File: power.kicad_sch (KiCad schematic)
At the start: 57 parts, among them Q6 2N7002K, U1 uA7805, U11 RT9080-33GJ5, U5 MIC5504, U6 DS4432U+, U6 INA219AID

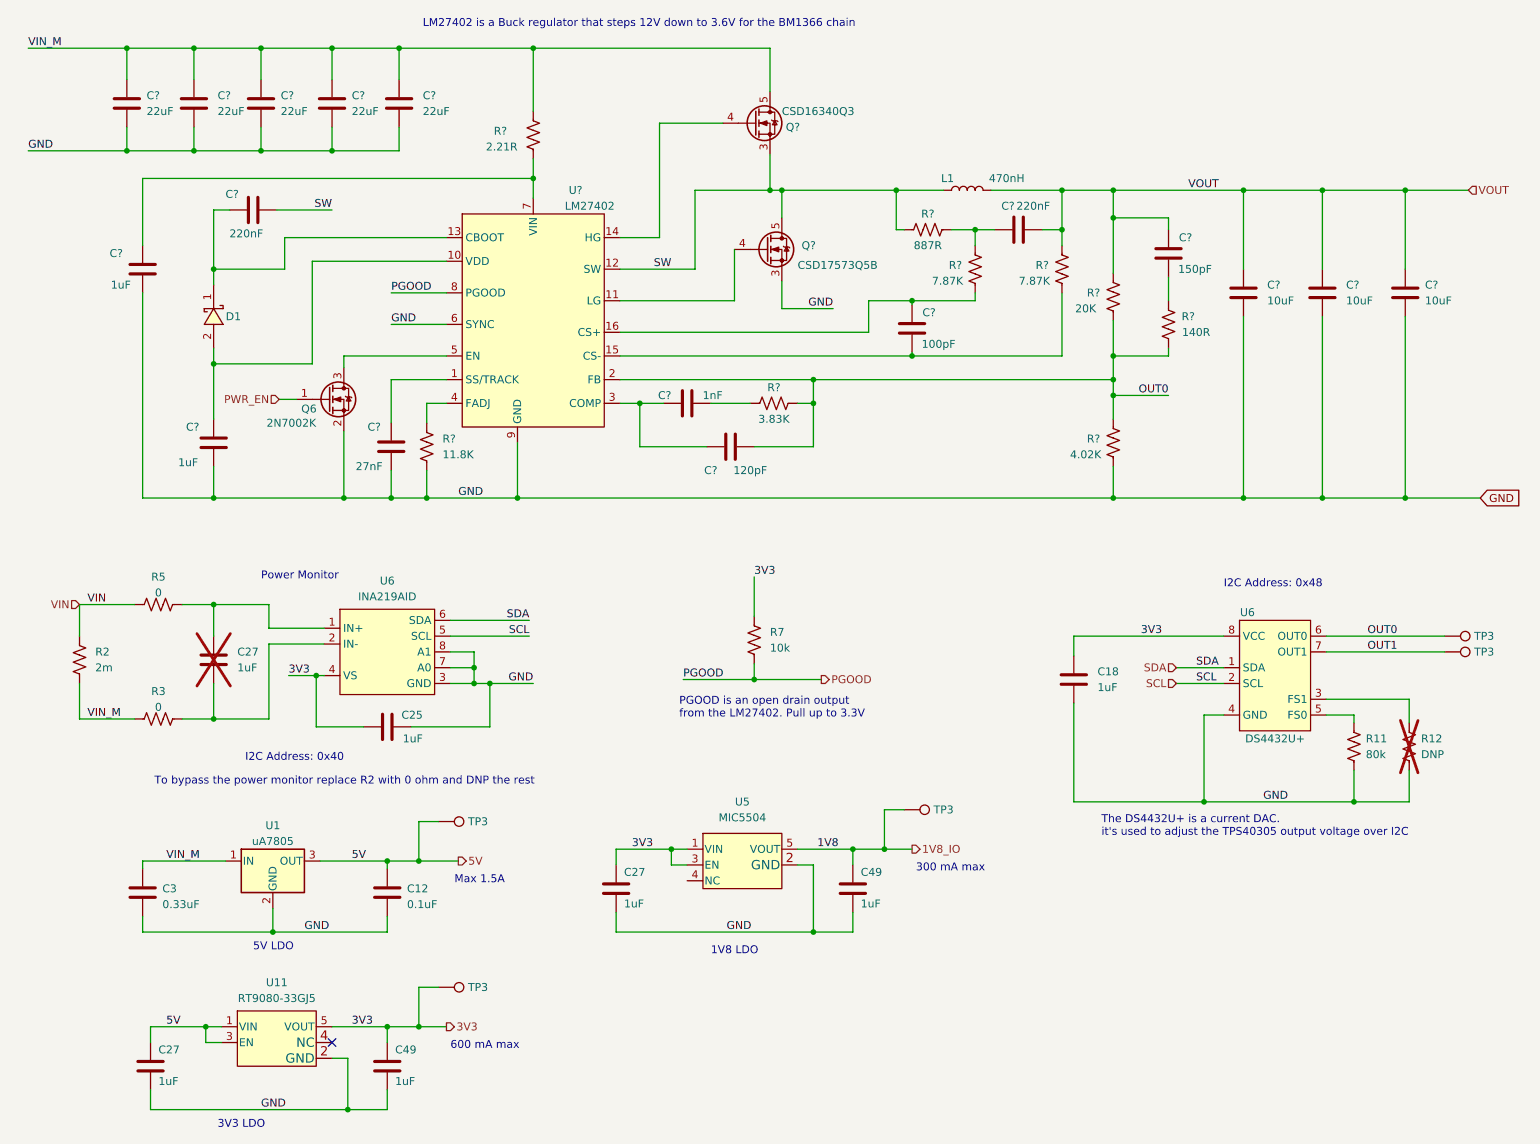
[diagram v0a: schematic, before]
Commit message: Create footprints for new MOSFETS, start on new power supply
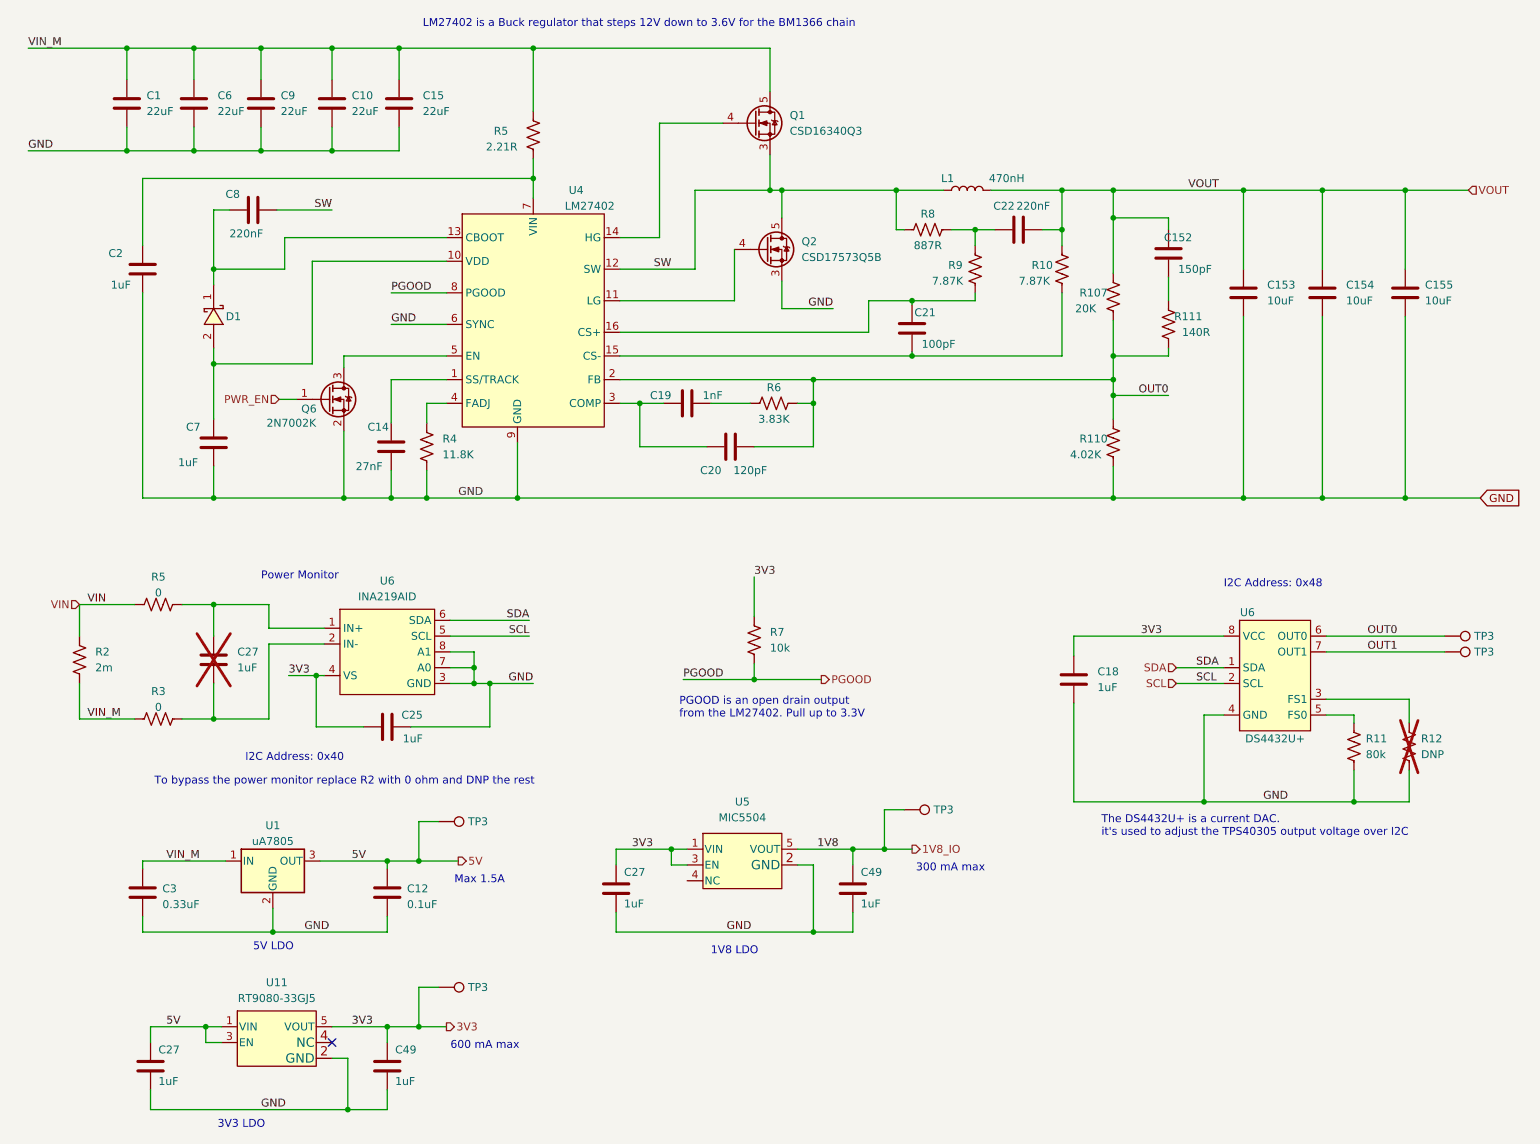
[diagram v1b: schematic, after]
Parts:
- removed Q?: CSD17573Q5B, symbol bitaxe:Q_NMOS_CSD17311Q5_1
- removed Q?: CSD16340Q3, symbol bitaxe:Q_NMOS_CSD17311Q5_1
- added Q1: CSD16340Q3, bitaxe:CSD16340Q3, symbol bitaxe:Q_NMOS_CSD16340Q3
- added Q2: CSD17573Q5B, bitaxe:CSD17573Q5B, symbol bitaxe:Q_NMOS_CSD17573Q5B
- gave numbers to parts that had none: 27
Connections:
- net GND: now also U4.17 (GND), Q2.1, Q2.2, Q2.3 (S)
- net SW: now also Q1.1, Q1.2, Q1.3 (S), Q2.5 (D)
- net VIN_M: now also Q1.5 (D)
- net at U4.11 (LG): now also Q2.4 (G)
- net at U4.14 (HG): now also Q1.4 (G)

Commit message: remove old 5V power supply, prepare footprints for new 5V buck supply, switch fans to 12V
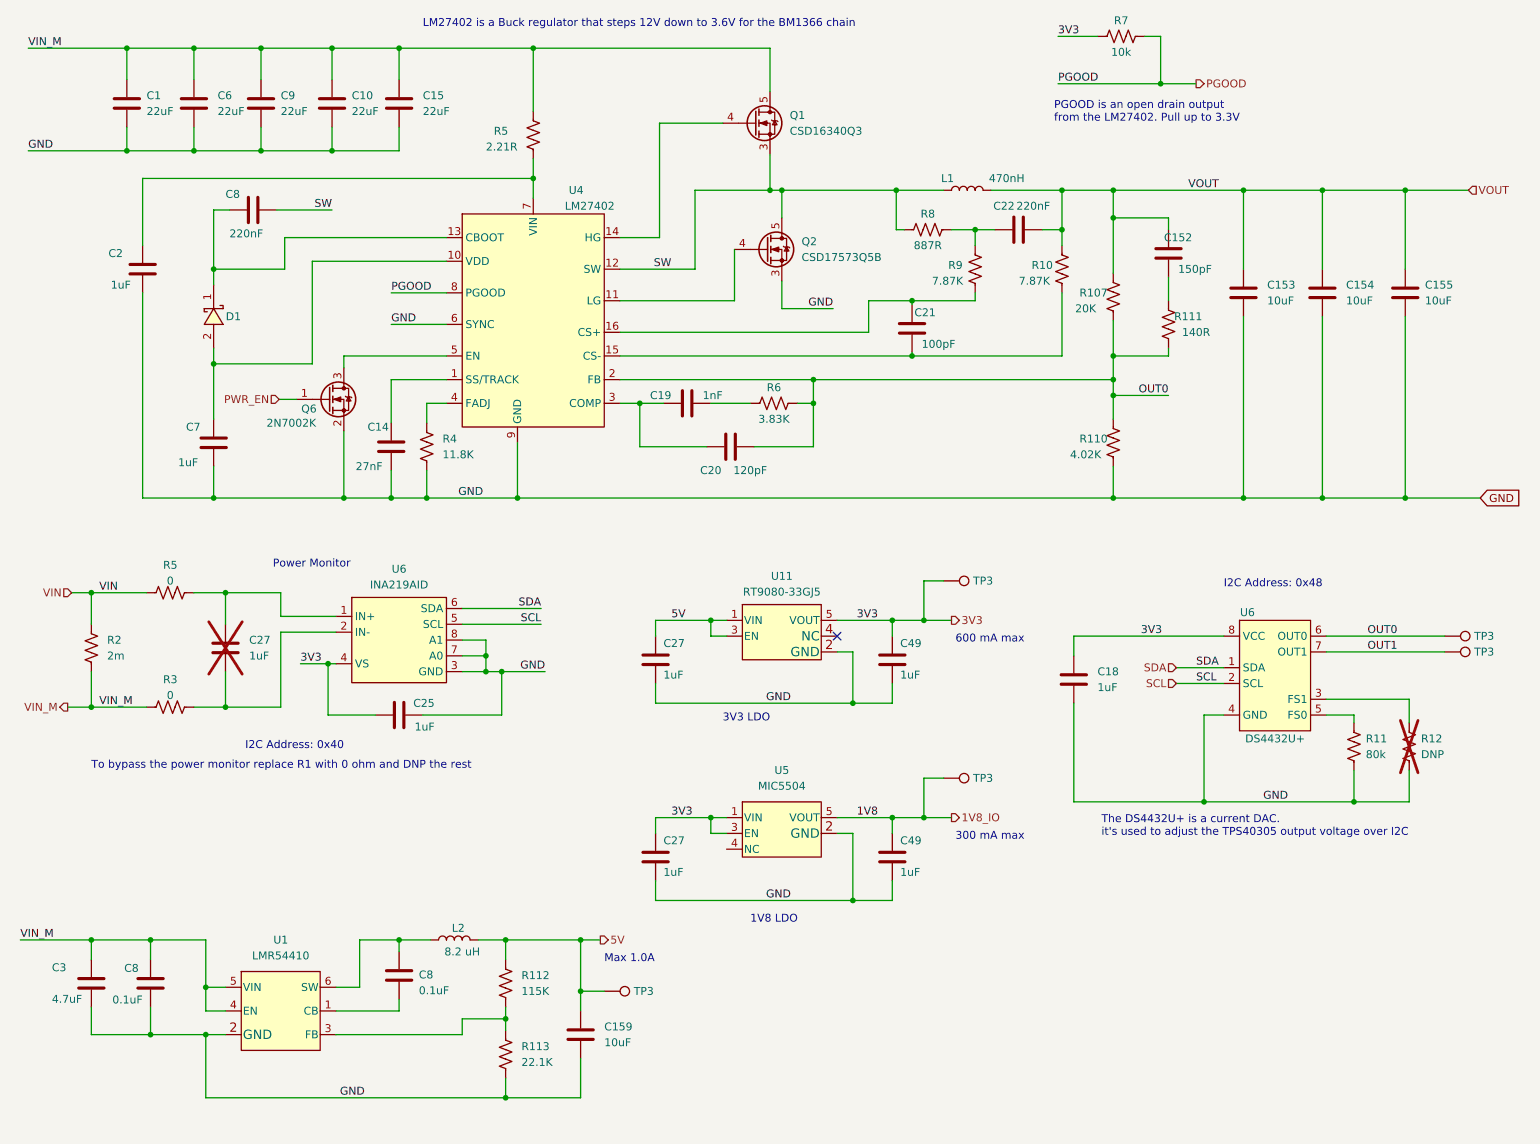
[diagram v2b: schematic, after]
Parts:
- removed C12: 0.1uF, Capacitor_SMD:C_0402_1005Metric, symbol Device:C
- removed U1: uA7805, Package_TO_SOT_SMD:TO-263-2, symbol Regulator_Linear:uA7805
- added C159: 10uF, Capacitor_SMD:C_0805_2012Metric, symbol Device:C
- added C8: 0.1uF, Capacitor_SMD:C_0402_1005Metric, symbol Device:C
- added C8: 0.1uF, Capacitor_SMD:C_0603_1608Metric, symbol Device:C
- added L2: 8.2 uH, bitaxe:74438357082, symbol Device:L
- added R112: 115K, Resistor_SMD:R_0402_1005Metric, symbol Device:R_US
- added R113: 22.1K, Resistor_SMD:R_0402_1005Metric, symbol Device:R_US
- added U1: LMR54410, Package_TO_SOT_SMD:SOT-23-6, symbol bitaxe:LMR54410
- C3: value 0.33uF -> 4.7uF; footprint Capacitor_SMD:C_0402_1005Metric -> Capacitor_SMD:C_1206_3216Metric; DK 490-GRM155R61J334ME01JCT-ND -> 490-6521-1-ND; PARTNO GRM155R61J334ME01J -> GRM31CR71H475KA12L
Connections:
- net 5V: now also C159.1, L2.2, R112.1
- net GND: now also C159.2, C8.1, R113.2, U1.2 (GND)
- net VIN_M: now also C8.2, U1.4 (EN), U1.5 (VIN)
- new net: C8.1, L2.1, U1.6 (SW)
- new net: C8.2, U1.1 (CB)
- new net: R112.2, R113.1, U1.3 (FB)
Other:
- note added: "Max 1.0A"
- note added: "To bypass the power monitor replace R1 with 0 ohm and DNP the rest"
- note removed: "5V LDO"
- note removed: "Max 1.5A"
- note removed: "To bypass the power monitor replace R2 with 0 ohm and DNP the rest"
- moved on the sheet: C25, C27, C49, R2, R3, R5, R7, TP3, U11, U5, U6

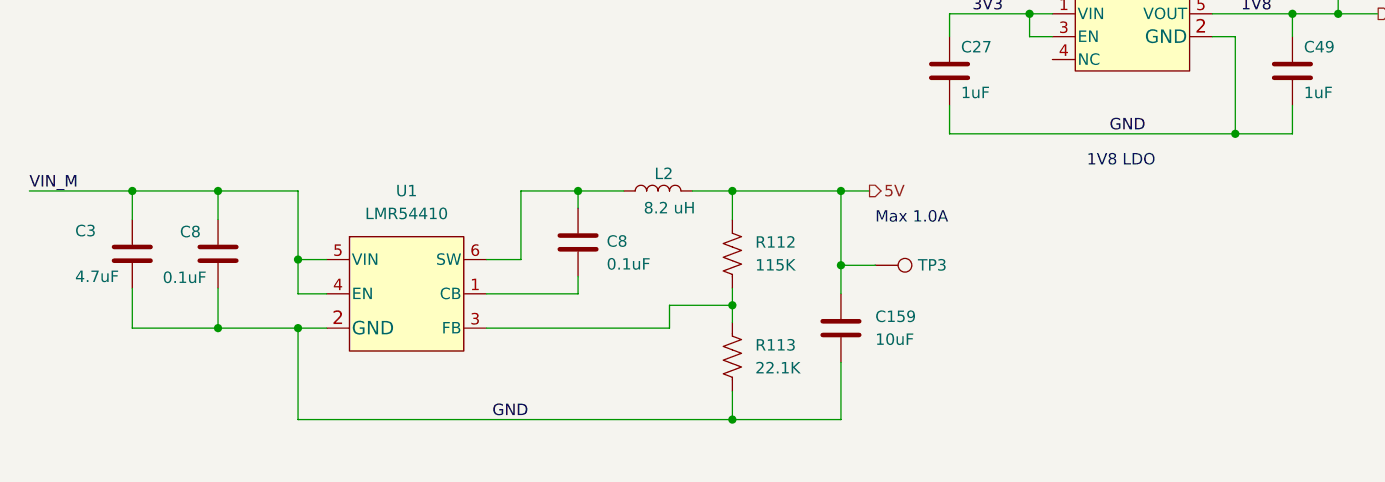
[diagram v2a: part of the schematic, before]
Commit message: shuffle capacitors on 5V buck regulator
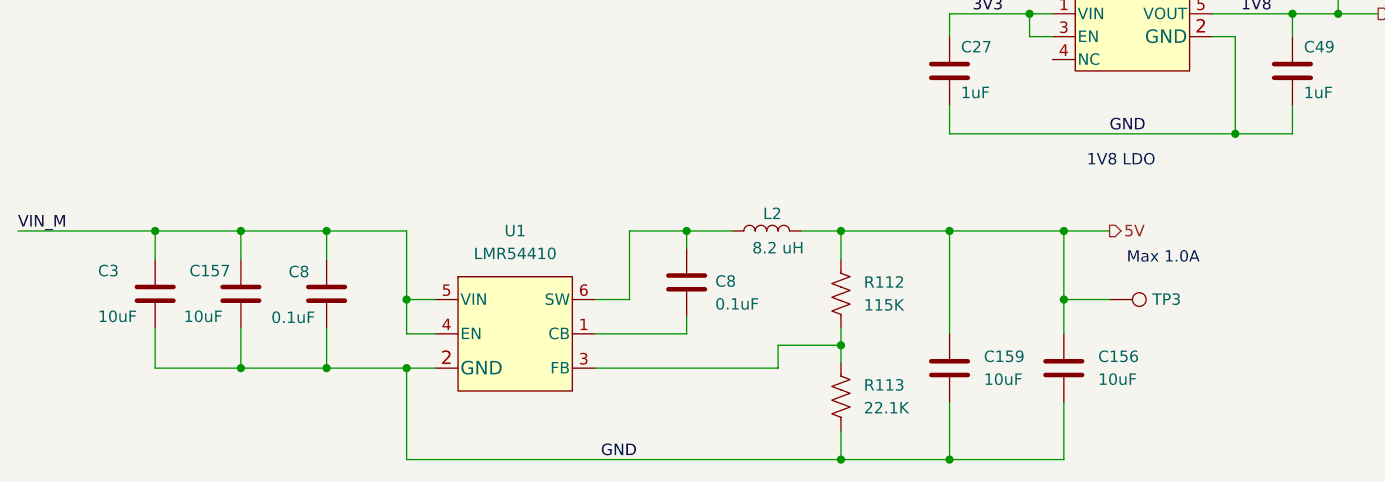
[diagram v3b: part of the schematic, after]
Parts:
- added C156, C157: 10uF, Capacitor_SMD:C_0805_2012Metric, symbol Device:C
- C3: value 4.7uF -> 10uF; footprint Capacitor_SMD:C_1206_3216Metric -> Capacitor_SMD:C_0805_2012Metric; DK 490-6521-1-ND -> 490-18664-1-ND; PARTNO GRM31CR71H475KA12L -> GRM21BR61H106ME43L
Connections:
- net 5V: now also C156.1
- net GND: now also C156.2, C157.2
- net VIN_M: now also C157.1
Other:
- moved on the sheet: C159, C8, L2, R112, R113, TP3, U1

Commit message: power supply work
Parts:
- removed C15: 22uF, Capacitor_SMD:C_1210_3225Metric, symbol Device:C
- added R114: 11.8K, Resistor_SMD:R_0402_1005Metric, symbol Device:R_US
- added TP3: TestPoint, TestPoint:TestPoint_Pad_D1.0mm, symbol Connector:TestPoint
- C19: footprint Capacitor_SMD:C_0805_2012Metric -> Capacitor_SMD:C_0402_1005Metric; DK 1276-2576-1-ND -> 490-3244-1-ND; PARTNO CL21C102JBCNFNC -> GRM1555C1H102JA01D
- Q1: value CSD16340Q3 -> CSD17303Q5; footprint bitaxe:CSD16340Q3 -> bitaxe:SON-Q5-MOSFET; DK 296-25646-1-ND -> 296-27232-1-ND; PARTNO CSD16340Q3 -> CSD17303Q5
- Q2: footprint bitaxe:CSD17573Q5B -> bitaxe:SON-Q5-MOSFET
- U4: footprint bitaxe:TPS40305 -> Package_DFN_QFN:WQFN-16-1EP_4x4mm_P0.5mm_EP2.6x2.6mm_ThermalVias
- U6: footprint Package_SO:SOIC-8_3.9x4.9mm_P1.27mm -> Package_TO_SOT_SMD:SOT-23-8
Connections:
- net 5V: now also R114.1
- net VOUT: now also TP3.1
- net at Q6.3 (D), U4.5 (EN): now also R114.2
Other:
- moved on the sheet: C1, C10, C2, C6, C7, C8, C9, D1
